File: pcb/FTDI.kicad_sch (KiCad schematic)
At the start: 51 parts, among them J3 USB3_B_micro, U3 FT600Q-B-x, U8 ECMF02-4CMX8, U9 ECMF04-4HSWM10, Y1 30MHz

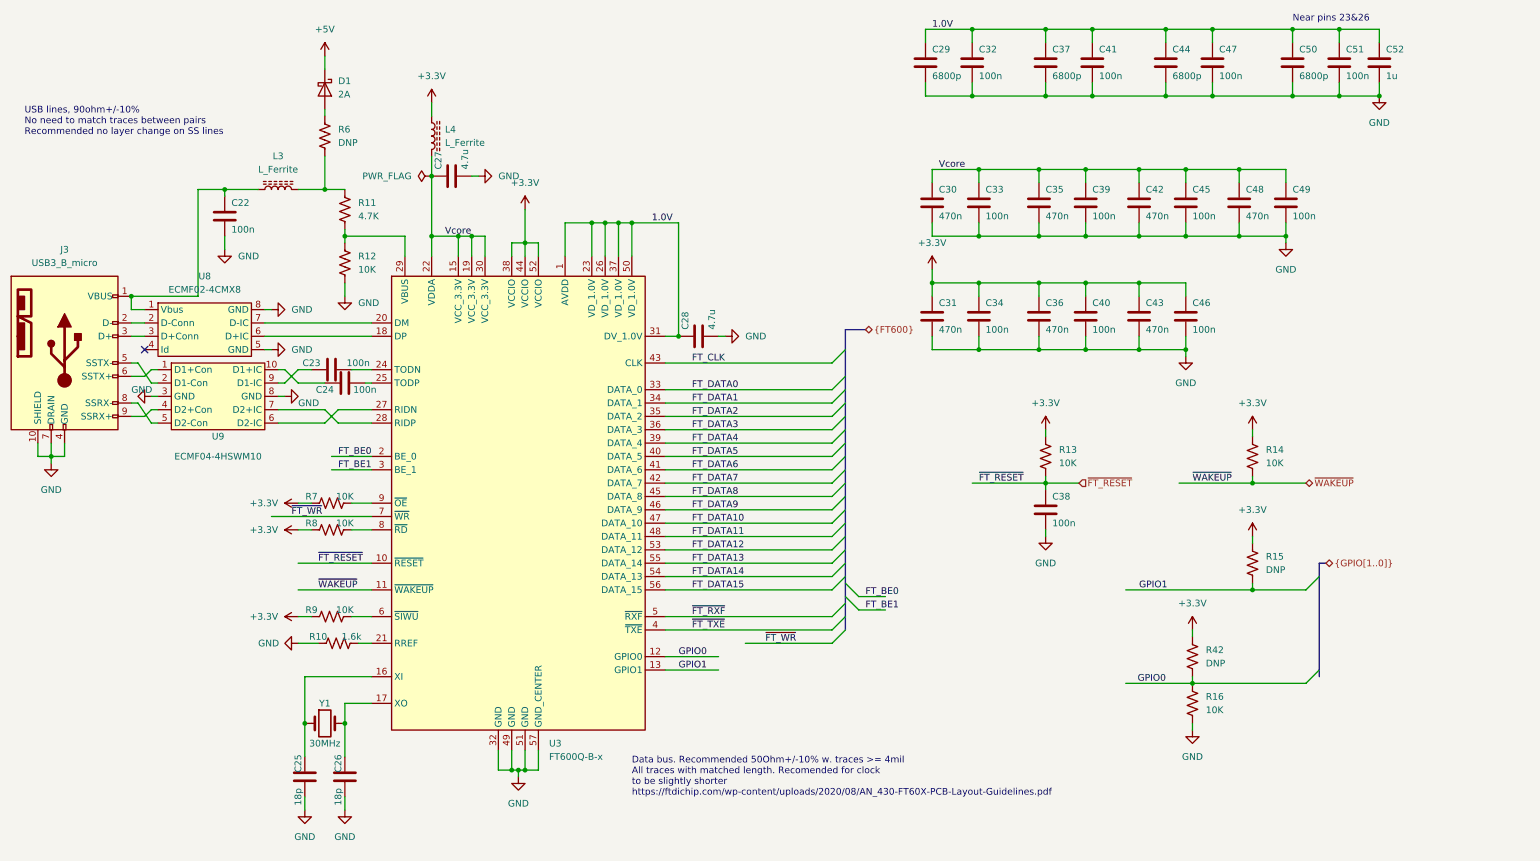
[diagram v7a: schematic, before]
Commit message: Initial footprint assignment
- Some edits to the schematic to improve readability
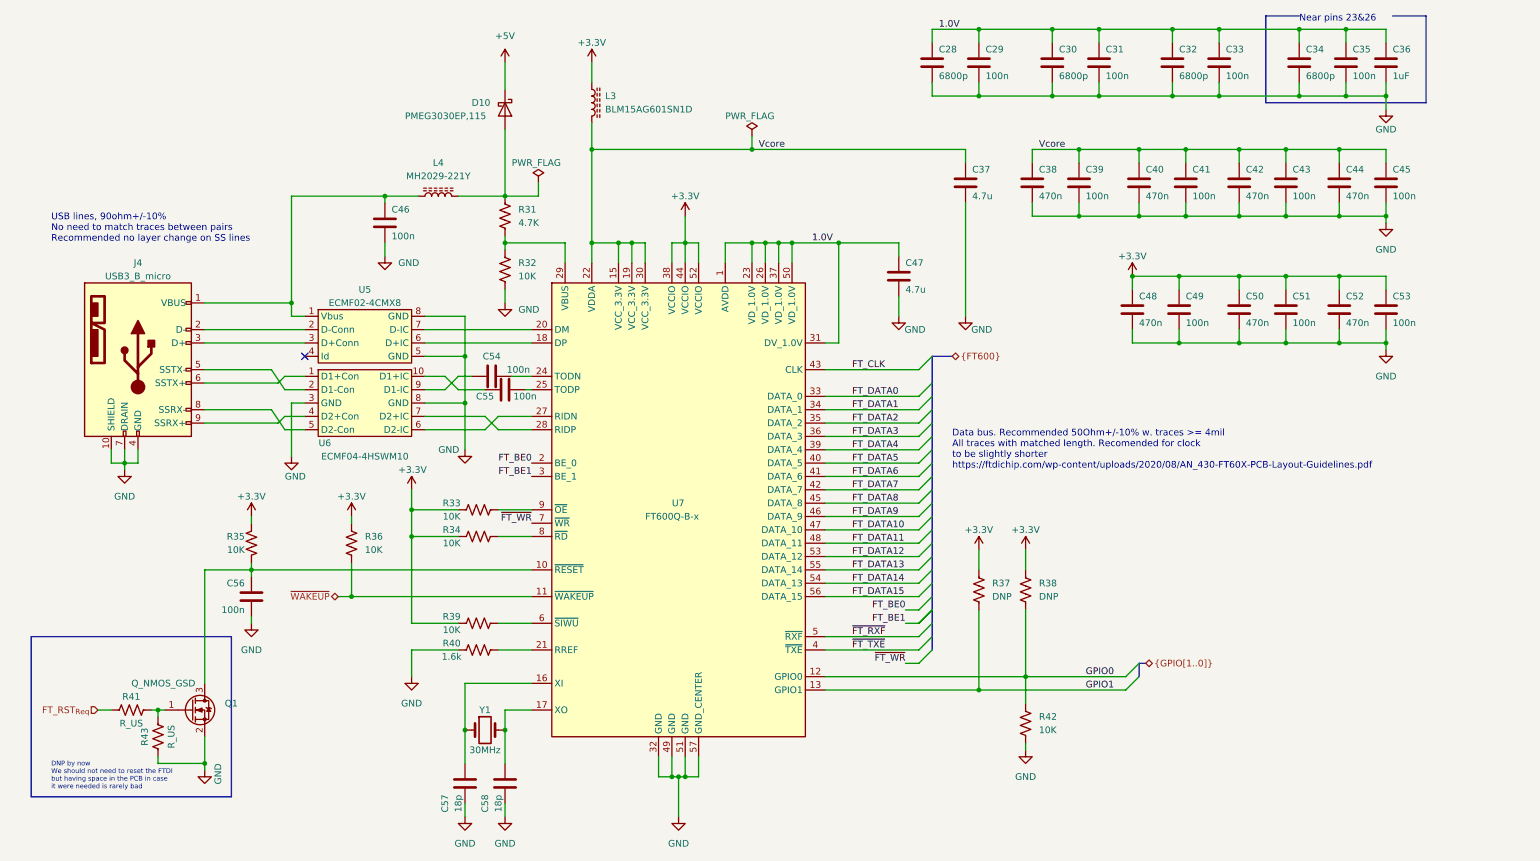
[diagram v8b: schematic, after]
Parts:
- removed D1: 2A, symbol Device:D_Schottky
- removed R6: DNP, symbol Device:R_US
- added D10: PMEG3030EP,115, Diode_SMD:D_SOD-128, symbol Device:D_Schottky
- added Q1: Q_NMOS_GSD, Package_TO_SOT_SMD:SOT-23, symbol Device:Q_NMOS_GSD
- added R41, R43: R_US, Resistor_SMD:R_0402_1005Metric, symbol Device:R_US
- C28: renamed from C29; footprint (none) -> Capacitor_SMD:C_0402_1005Metric
- C29: renamed from C32; footprint (none) -> Capacitor_SMD:C_0402_1005Metric
- C30: renamed from C37; footprint (none) -> Capacitor_SMD:C_0402_1005Metric
- C31: renamed from C41; footprint (none) -> Capacitor_SMD:C_0402_1005Metric
- C32: renamed from C44; footprint (none) -> Capacitor_SMD:C_0402_1005Metric
- C33: renamed from C47; footprint (none) -> Capacitor_SMD:C_0402_1005Metric
- C34: renamed from C50; footprint (none) -> Capacitor_SMD:C_0402_1005Metric
- C35: renamed from C51; footprint (none) -> Capacitor_SMD:C_0402_1005Metric
- C36: renamed from C52; value 1u -> 1uF; footprint (none) -> Capacitor_SMD:C_0805_2012Metric
- C37: renamed from C27; footprint (none) -> Capacitor_SMD:C_1210_3225Metric
- C38: renamed from C30; footprint (none) -> Capacitor_SMD:C_0402_1005Metric
- C39: renamed from C33; footprint (none) -> Capacitor_SMD:C_0402_1005Metric
- C40: renamed from C35; footprint (none) -> Capacitor_SMD:C_0402_1005Metric
- C41: renamed from C39; footprint (none) -> Capacitor_SMD:C_0402_1005Metric
- C42: footprint (none) -> Capacitor_SMD:C_0402_1005Metric
- C43: renamed from C45; footprint (none) -> Capacitor_SMD:C_0402_1005Metric
- C44: renamed from C48; footprint (none) -> Capacitor_SMD:C_0402_1005Metric
- C45: renamed from C49; footprint (none) -> Capacitor_SMD:C_0402_1005Metric
- C46: renamed from C22; footprint (none) -> Capacitor_SMD:C_0402_1005Metric
- C47: renamed from C28; footprint (none) -> Capacitor_SMD:C_1210_3225Metric
- C48: renamed from C31; footprint (none) -> Capacitor_SMD:C_0402_1005Metric
- C49: renamed from C34; footprint (none) -> Capacitor_SMD:C_0402_1005Metric
- C50: renamed from C36; footprint (none) -> Capacitor_SMD:C_0402_1005Metric
- C51: renamed from C40; footprint (none) -> Capacitor_SMD:C_0402_1005Metric
- C52: renamed from C43; footprint (none) -> Capacitor_SMD:C_0402_1005Metric
- C53: renamed from C46; footprint (none) -> Capacitor_SMD:C_0402_1005Metric
- C54: renamed from C23; footprint (none) -> Capacitor_SMD:C_0402_1005Metric
- C55: renamed from C24; footprint (none) -> Capacitor_SMD:C_0402_1005Metric
- C56: renamed from C38; footprint (none) -> Capacitor_SMD:C_0402_1005Metric
- C57: renamed from C25; footprint (none) -> Capacitor_SMD:C_0402_1005Metric
- C58: renamed from C26; footprint (none) -> Capacitor_SMD:C_0402_1005Metric
- J4: renamed from J3; footprint (none) -> Connector_USB:USB_Micro-B_Wuerth_629105150521
- L3: renamed from L4; value L_Ferrite -> BLM15AG601SN1D; footprint (none) -> Inductor_SMD:L_0402_1005Metric
- L4: renamed from L3; value L_Ferrite -> MH2029-221Y; footprint (none) -> Inductor_SMD:L_0805_2012Metric
- R31: renamed from R11; footprint (none) -> Resistor_SMD:R_0402_1005Metric
- R32: renamed from R12; footprint (none) -> Resistor_SMD:R_0402_1005Metric
- R33: renamed from R7; footprint (none) -> Resistor_SMD:R_0402_1005Metric
- R34: renamed from R8; footprint (none) -> Resistor_SMD:R_0402_1005Metric
- R35: renamed from R13; footprint (none) -> Resistor_SMD:R_0402_1005Metric
- R36: renamed from R14; footprint (none) -> Resistor_SMD:R_0402_1005Metric
- R37: renamed from R15; footprint (none) -> Resistor_SMD:R_0402_1005Metric
- R38: renamed from R42; footprint (none) -> Resistor_SMD:R_0402_1005Metric
- R39: renamed from R9; footprint (none) -> Resistor_SMD:R_0402_1005Metric
- R40: renamed from R10; footprint (none) -> Resistor_SMD:R_0402_1005Metric
- R42: renamed from R16; footprint (none) -> Resistor_SMD:R_0402_1005Metric
- U5: renamed from U8; footprint (none) -> jonnew:ST_MICROQFN-8L-2.5x1.15x0.45
- U6: renamed from U9; footprint (none) -> jonnew:ST_QFN10L-2.6x1.35x0.5
- Y1: footprint (none) -> Crystal:Crystal_SMD_5032-4Pin_5.0x3.2mm
- renumbered U3 to U7
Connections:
- net +5V: now also D10.1 (K)
- net GND: now also Q1.2 (S), R43.1
- net at L4.2, R31.1: now also D10.2 (A)
- net ~{FT_RESET}: no longer names the net of C56.1, R35.2, U7.10 (~{RESET})
- net ~{FT_RESET}: now also Q1.3 (D)
- new net: Q1.1 (G), R41.2, R43.2
- new net FT_RST_{Req}: R41.1
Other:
- note added: "DNP by now We should not need to reset the FTDI but having space in the PCB in case it were needed is rarely bad"
- company: OEPS -> OEPS & Open Ephys, Inc.
- title: ECP5U85-BSE-USB Breakout board -> ECP5U85-BSE-USB Breakout Board
- moved on the sheet: C28, C29, C30, C31, C32, C33, C34, C35, C36, C37, C38, C39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
